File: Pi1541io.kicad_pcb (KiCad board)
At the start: 2 copper layers, 65 x 56 mm, 51 parts, among them J1 IEC1, J10 SDA, J11 SCL, J12 I2C, J2 IEC2, J3 IEC3, J4 ExtSpkr, J5 GS3, J6 GS3, J7 GS3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

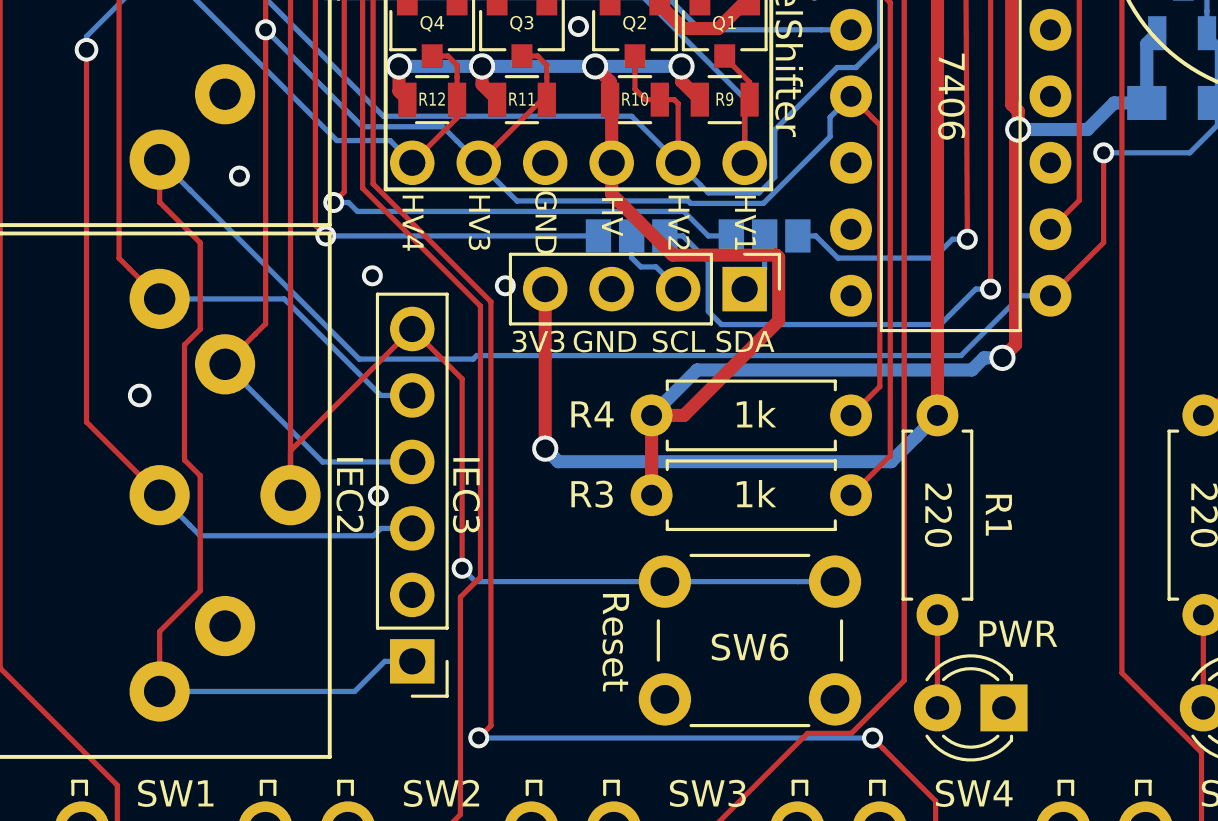
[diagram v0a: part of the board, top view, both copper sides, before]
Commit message: I2C power pins now configurable.
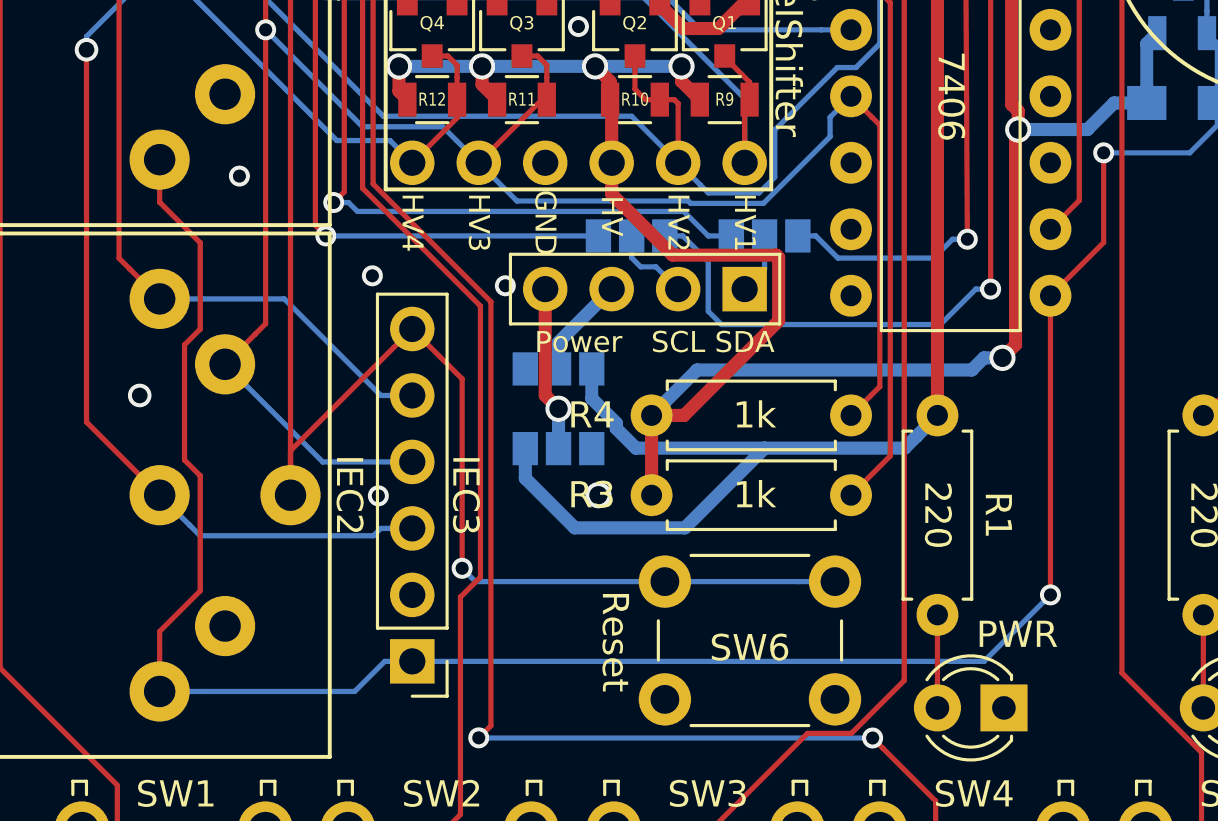
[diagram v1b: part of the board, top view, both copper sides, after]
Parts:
- added J13: SDA, Connectors:GS3, B.Cu at (132.8, 92.6)
- added J14: SDA, Connectors:GS3, B.Cu at (132.8, 95.6)
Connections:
- J12 pad 3: GND -> Net-(J12-Pad3)
- J12 pad 4: +3V3 -> Net-(J12-Pad4)
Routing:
- net Net-(J12-Pad4): track 0.00 -> 6.31 mm, vias 0 -> 1
- net +3V3: track 123.6 -> 129.6 mm
- net Net-(J12-Pad3): track 0.00 -> 3.89 mm
- net SRQ: track 87.6 -> 86.3 mm, vias 1 -> 2
- net GND: vias 11 -> 12
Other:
- board text added: "GND- Vcc"
- board text added: "Power"
- board text added: "Vcc- GND"
- board text removed: "3V3"
- board text removed: "GND"

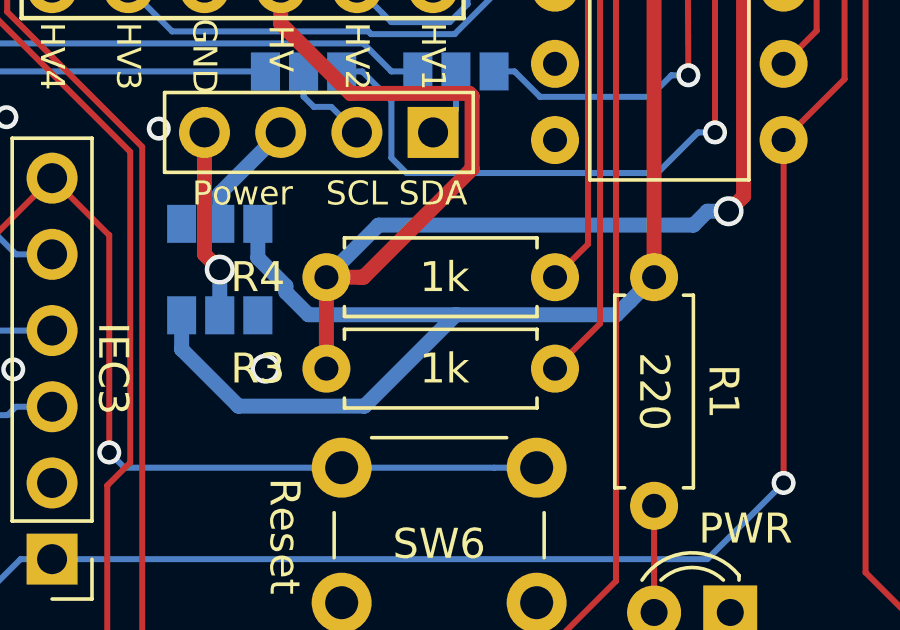
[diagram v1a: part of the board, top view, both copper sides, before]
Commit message: Both voltage and pin order now configurable.
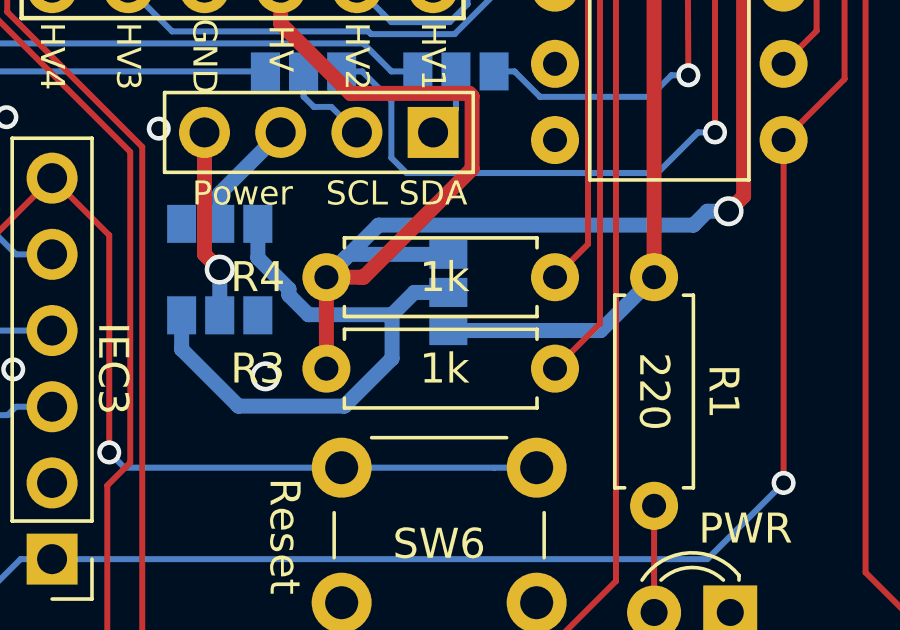
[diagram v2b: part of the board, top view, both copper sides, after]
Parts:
- added J15: SDA, Connectors:GS3, B.Cu at (140.4, 94.9)
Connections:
- J13 pad 1: +3V3 -> Net-(J13-Pad1)
- J14 pad 1: +3V3 -> Net-(J13-Pad1)
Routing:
- net +3V3: track 129.6 -> 109.2 mm, vias 5 -> 4
- net Net-(J13-Pad1): track 0.00 -> 19.7 mm
- net +5V: track 135.0 -> 139.4 mm
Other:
- board text added: "3V3"
- board text added: "5V"
- board text added: "Bus 0 1"
- board text added: "I2C Config"
- board text removed: "I2C 0 1"
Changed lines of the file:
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@@
-(kicad_pcb (version 20171130) (host pcbnew "(5.0.0-rc2-154-gb82bf7c44)")
+(kicad_pcb (version 20171130) (host pcbnew "(5.0.0-rc2-dev-406-g05dae9627)")
   (general
     (thickness 1.6)
-    (drawings 107)
-    (tracks 554)
+    (drawings 115)
+    (tracks 557)
     (zones 0)
-    (modules 53)
-    (nets 49)
+    (modules 54)
+    (nets 50)
   )
   (page A4)
   (title_block
     (title "Pi1541 IO Adapter")
-    (date 2018-07-05)
+    (date 2018-07-08)
     (rev 4)
     (company hackup.net)
@@
       (hpglpennumber 1)
       (hpglpenspeed 20)
-      (hpglpendiameter 15.000000)
+      (hpglpendiameter 15)
       (psnegative false)
       (psa4output false)
@@
   (net 47 "Net-(J12-Pad3)")
   (net 48 "Net-(J12-Pad4)")
+  (net 49 "Net-(J13-Pad1)")
   (net_class Default "This is the default net class."
     (clearance 0.2)
@@
     (add_net "Net-(J12-Pad3)")
     (add_net "Net-(J12-Pad4)")
+    (add_net "Net-(J13-Pad1)")
   )
   (module Socket_Strips:Socket_Strip_Straight_1x04_Pitch2.54mm (layer F.Cu)
@@
     (fp_line (start -1.15 -2.15) (end -1.15 2.15) (layer B.CrtYd) (width 0.05))
     (pad 1 smd rect (at 0 1.27 90) (size 1.27 0.97) (layers B.Cu B.Paste B.Mask)
-      (net 1 +3V3))
+      (net 49 "Net-(J13-Pad1)"))
     (pad 2 smd rect (at 0 0 90) (size 1.27 0.97) (layers B.Cu B.Paste B.Mask)
       (net 47 "Net-(J12-Pad3)"))
@@
       (net 48 "Net-(J12-Pad4)"))
     (pad 1 smd rect (at 0 1.27 270) (size 1.27 0.97) (layers B.Cu B.Paste B.Mask)
-      (net 1 +3V3))
+      (net 49 "Net-(J13-Pad1)"))
   )
   (module Pin_Headers:Pin_Header_Straight_1x02_Pitch2.54mm (layer F.Cu)
@@
       (net 42 I2C1_SCL))
   )
+  (module Connectors:GS3 (layer B.Cu)
+    (at 140.437 94.882)
+    (descr "3-pin solder bridge")
+    (tags "solder bridge")
+    (attr smd)
+    (fp_text reference J15 (at -1.7 0 -90) (layer B.SilkS) hide
+      (effects (font (size 1 1) (thickness 0.15)) (justify mirror))
+    )
+    (fp_text value SDA (at 1.8 0 -90) (layer B.Fab)
+      (effects (font (size 1 1) (thickness 0.15)) (justify mirror))
+    )
+    (fp_line (start -1.15 2.15) (end 1.15 2.15) (layer B.CrtYd) (width 0.05))
+    (fp_line (start 1.15 2.15) (end 1.15 -2.15) (layer B.CrtYd) (width 0.05))
+    (fp_line (start 1.15 -2.15) (end -1.15 -2.15) (layer B.CrtYd) (width 0.05))
+    (fp_line (start -1.15 -2.15) (end -1.15 2.15) (layer B.CrtYd) (width 0.05))
+    (fp_line (start -0.89 1.91) (end -0.89 -1.91) (layer B.SilkS) (width 0.12))
+    (fp_line (start -0.89 -1.91) (end 0.89 -1.91) (layer B.SilkS) (width 0.12))
+    (fp_line (start 0.89 -1.91) (end 0.89 1.91) (layer B.SilkS) (width 0.12))
+    (fp_line (start -0.89 1.91) (end 0.89 1.91) (layer B.SilkS) (width 0.12))
+    (pad 1 smd rect (at 0 1.27) (size 1.27 0.97) (layers B.Cu B.Paste B.Mask)
+      (net 1 +3V3))
+    (pad 2 smd rect (at 0 0) (size 1.27 0.97) (layers B.Cu B.Paste B.Mask)
+      (net 49 "Net-(J13-Pad1)"))
+    (pad 3 smd rect (at 0 -1.27) (size 1.27 0.97) (layers B.Cu B.Paste B.Mask)
+      (net 2 +5V))
+  )
+  (gr_text "I2C Config" (at 139.421 102.502) (layer B.SilkS)
+    (effects (font (size 0.8 0.8) (thickness 0.2)) (justify mirror))
+  )
+  (gr_line (start 128.372 85.865) (end 142.85 85.865) (layer B.SilkS) (width 0.1))
+  (gr_line (start 142.85 99.454) (end 142.85 85.865) (layer B.SilkS) (width 0.1))
+  (gr_line (start 142.85 103.391) (end 142.85 101.994) (layer B.SilkS) (width 0.1))
+  (gr_line (start 128.372 103.391) (end 142.85 103.391) (layer B.SilkS) (width 0.1))
+  (gr_line (start 128.372 85.865) (end 128.372 103.391) (layer B.SilkS) (width 0.1))
+  (gr_text 3V3 (at 140.437 97.549) (layer B.SilkS)
+    (effects (font (size 0.8 0.8) (thickness 0.15)) (justify mirror))
+  )
+  (gr_text 5V (at 140.437 92.342) (layer B.SilkS)
+    (effects (font (size 0.8 0.8) (thickness 0.15)) (justify mirror))
+  )
   (gr_line (start 133.96 96.787) (end 133.96 100.597) (layer B.SilkS) (width 0.1))
   (gr_line (start 131.674 96.787) (end 131.674 97.549) (layer B.SilkS) (width 0.1))
@@
   (gr_line (start 131.547 85.992) (end 131.547 88.659) (layer B.SilkS) (width 0.1))
   (gr_line (start 128.499 85.992) (end 131.547 85.992) (layer B.SilkS) (width 0.1))
-  (gr_text "I2C\n0  1" (at 130.023 87.389) (layer B.SilkS)
+  (gr_text "Bus\n0  1" (at 130.023 87.389) (layer B.SilkS)
     (effects (font (size 0.8 0.8) (thickness 0.15)) (justify mirror))
   )
@@
   (segment (start 148.002106 76.086) (end 148.236107 75.851999) (width 0.5) (layer B.Cu) (net 1))
   (segment (start 147.295 76.086) (end 148.002106 76.086) (width 0.5) (layer B.Cu) (net 1))
-  (via (at 147.295 94.374) (size 1) (drill 0.7) (layers F.Cu B.Cu) (net 1))
-  (segment (start 146.495001 95.173999) (end 147.295 94.374) (width 0.5) (layer B.Cu) (net 1))
-  (segment (start 146.044999 95.624001) (end 146.495001 95.173999) (width 0.5) (layer B.Cu) (net 1))
-  (segment (start 135.022001 94.873003) (end 135.772999 95.624001) (width 0.5) (layer B.Cu) (net 1))
-  (segment (start 135.022001 94.666001) (end 135.022001 94.873003) (width 0.5) (layer B.Cu) (net 1))
-  (segment (start 134.087 93.731) (end 135.022001 94.666001) (width 0.5) (layer B.Cu) (net 1))
-  (segment (start 134.087 92.596) (end 134.087 93.731) (width 0.5) (layer B.Cu) (net 1))
-  (segment (start 137.643 98.672001) (end 140.691 95.624001) (width 0.5) (layer B.Cu) (net 1))
-  (segment (start 133.440001 98.672001) (end 137.643 98.672001) (width 0.5) (layer B.Cu) (net 1))
-  (segment (start 131.547 96.779) (end 133.440001 98.672001) (width 0.5) (layer B.Cu) (net 1))
-  (segment (start 131.547 95.644) (end 131.547 96.779) (width 0.5) (layer B.Cu) (net 1))
-  (segment (start 135.772999 95.624001) (end 140.691 95.624001) (width 0.5) (layer B.Cu) (net 1))
-  (segment (start 140.691 95.624001) (end 146.044999 95.624001) (width 0.5) (layer B.Cu) (net 1))
+  (segment (start 145.517 96.152) (end 140.437 96.152) (width 0.5) (layer B.Cu) (net 1))
+  (segment (start 147.295 94.374) (end 145.517 96.152) (width 0.5) (layer B.Cu) (net 1))
   (segment (start 114.517 61.432) (end 117.057 61.432) (width 0.5) (layer B.Cu) (net 2) (status 30))
   (segment (start 151.613 74.562) (end 151.613 69.99) (width 0.5) (layer F.Cu) (net 2))
@@
   (segment (start 134.849 85.924081) (end 137.172918 88.247999) (width 0.5) (layer F.Cu) (net 2))
   (segment (start 134.849 84.722) (end 134.849 85.924081) (width 0.5) (layer F.Cu) (net 2))
+  (segment (start 137.135 93.612) (end 136.373 94.374) (width 0.5) (layer B.Cu) (net 2))
+  (segment (start 140.437 93.612) (end 137.135 93.612) (width 0.5) (layer B.Cu) (net 2))
   (via (at 116.815 93.612) (size 0.9) (drill 0.6) (layers F.Cu B.Cu) (net 3))
   (via (at 146.914 66.307) (size 0.8) (drill 0.5) (layers F.Cu B.Cu) (net 3))
@@
   (via (at 120.625 85.23) (size 0.8) (drill 0.5) (layers F.Cu B.Cu) (net 3))
   (via (at 130.785 89.421) (size 0.8) (drill 0.5) (layers F.Cu B.Cu) (net 3))
-  (via (at 134.341 97.422) (size 1) (drill 0.7) (layers F.Cu B.Cu) (net 3))
+  (via (at 134.341 97.679011) (size 1) (drill 0.7) (layers F.Cu B.Cu) (net 3))
   (segment (start 154.345002 68.240002) (end 150.926999 64.821999) (width 0.2) (layer F.Cu) (net 4))
   (segment (start 150.926999 64.821999) (end 150.077 63.972) (width 0.2) (layer F.Cu) (net 4))
@@
   (segment (start 132.309 93.612) (end 132.817 94.12) (width 0.5) (layer F.Cu) (net 48))
   (segment (start 132.817 94.12) (end 132.817 95.644) (width 0.5) (layer B.Cu) (net 48))
+  (segment (start 134.087 93.731) (end 134.087 92.596) (width 0.5) (layer B.Cu) (net 49))
+  (segment (start 135.122999 94.766999) (end 134.087 93.731) (width 0.5) (layer B.Cu) (net 49))
+  (segment (start 135.122999 94.974001) (end 135.122999 94.766999) (width 0.5) (layer B.Cu) (net 49))
+  (segment (start 135.772999 95.624001) (end 135.122999 94.974001) (width 0.5) (layer B.Cu) (net 49))
+  (segment (start 138.559999 95.624001) (end 135.772999 95.624001) (width 0.5) (layer B.Cu) (net 49))
+  (segment (start 139.302 94.882) (end 138.559999 95.624001) (width 0.5) (layer B.Cu) (net 49))
+  (segment (start 140.437 94.882) (end 139.302 94.882) (width 0.5) (layer B.Cu) (net 49))
+  (segment (start 138.559999 97.085003) (end 138.559999 95.624001) (width 0.5) (layer B.Cu) (net 49))
+  (segment (start 136.973001 98.672001) (end 138.559999 97.085003) (width 0.5) (layer B.Cu) (net 49))
+  (segment (start 133.440001 98.672001) (end 136.973001 98.672001) (width 0.5) (layer B.Cu) (net 49))
+  (segment (start 131.547 96.779) (end 133.440001 98.672001) (width 0.5) (layer B.Cu) (net 49))
+  (segment (start 131.547 95.644) (end 131.547 96.779) (width 0.5) (layer B.Cu) (net 49))
   (zone (net 3) (net_name GND) (layer F.Cu) (hatch edge 0.508)
     (connect_pads (clearance 0.4))

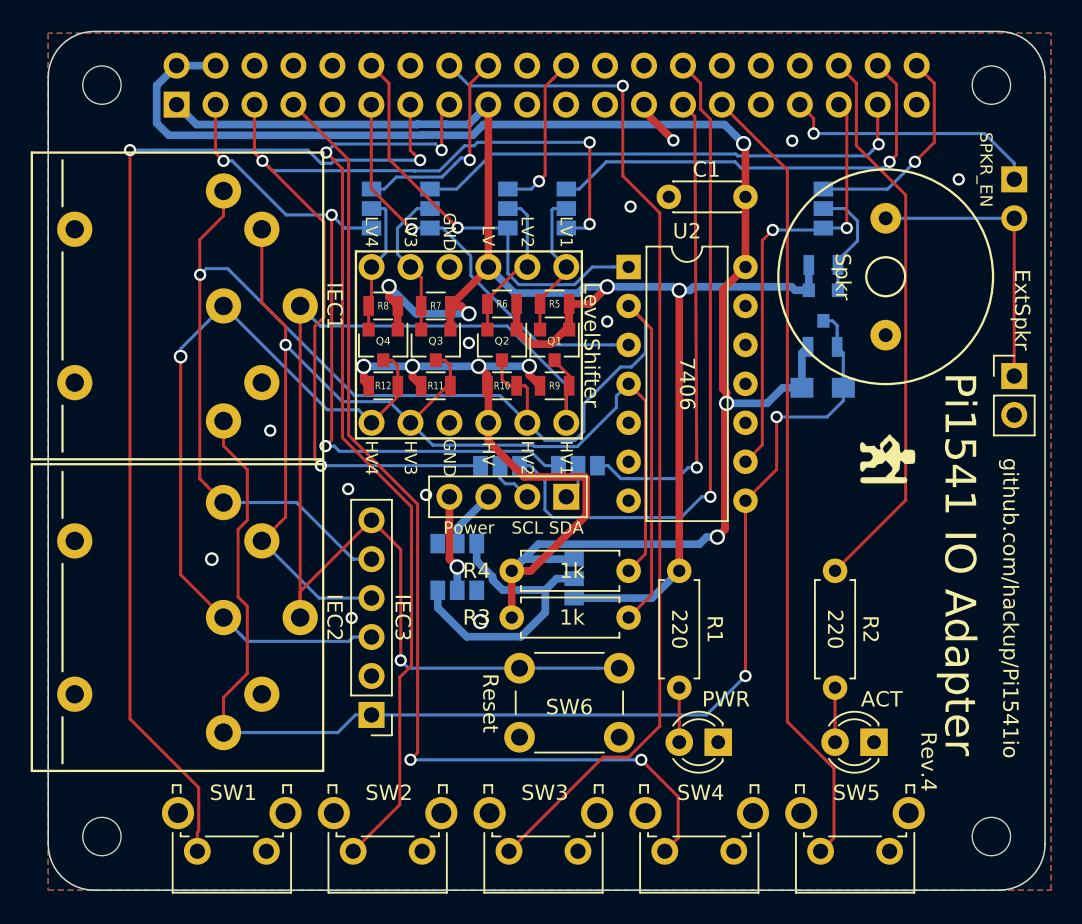
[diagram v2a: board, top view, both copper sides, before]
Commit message: Added additional drill holes for DIN connectors and polarity indicator for LEDs.
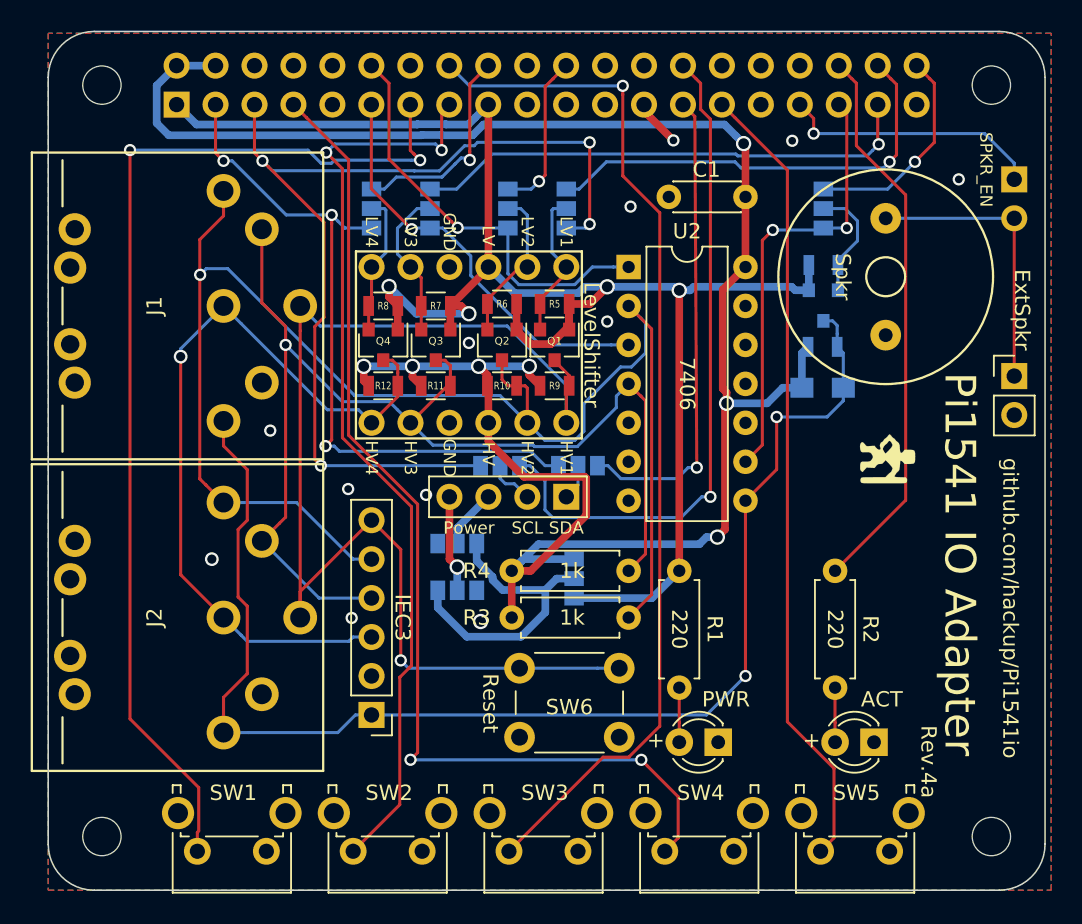
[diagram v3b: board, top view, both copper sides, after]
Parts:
- J1, J2: footprint DIN-Connector:DIN-6 -> DIN-Connector:DIN-6-Variable
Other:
- board text added: "+"
- board text added: "Rev.4a"
- board text removed: "Rev.4"
